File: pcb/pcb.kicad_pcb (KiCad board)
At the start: 2 copper layers, 84 parts, among them J1 MJ-4PP-9, J2 MJ-4PP-9, SW1 KEY_SW, SW10 KEY_SW, SW11 KEY_SW, SW12 KEY_SW, SW13 KEY_SW, SW14 KEY_SW, SW15 KEY_SW, SW16 KEY_SW, SW17 KEY_SW, SW18 KEY_SW, SW19 KEY_SW, SW2 KEY_SW, SW20 KEY_SW, SW21 KEY_SW, SW22 KEY_SW, SW23 KEY_SW, SW24 KEY_SW, SW25 KEY_SW, SW26 KEY_SW, SW27 RotaryEncoder, SW3 KEY_SW, SW30 KEY_SW, SW31 KEY_SW, SW32 KEY_SW, SW33 KEY_SW, SW34 KEY_SW, SW35 KEY_SW, SW36 KEY_SW, SW37 KEY_SW, SW38 KEY_SW, SW39 KEY_SW, SW4 KEY_SW, SW40 KEY_SW, SW41 KEY_SW, SW42 KEY_SW, SW43 KEY_SW, SW44 KEY_SW, SW45 KEY_SW, SW46 KEY_SW, SW47 KEY_SW, SW48 KEY_SW, SW49 KEY_SW, SW5 KEY_SW, SW50 KEY_SW, SW51 KEY_SW, SW52 KEY_SW, SW53 KEY_SW, SW54 KEY_SW, SW55 RotaryEncoder, SW6 KEY_SW, SW7 KEY_SW, SW8 KEY_SW, SW9 KEY_SW, U1 ESP32-S3-WROOM-1, U3 USBLC6-2SC6

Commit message: switch put to pcb
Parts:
- removed SW55: RotaryEncoder, keebio:RotaryEncoder_EC11
- added ?: , , F.Cu at (103.2, 117.0)
- added BT1: Battery_Cell, Connector_JST:JST_XH_S2B-XH-A_1x02_P2.50mm_Horizontal, F.Cu at (20.0, -34.4)
- added C1: 0.1uF, Capacitor_SMD:C_0805_2012Metric_Pad1.18x1.45mm_HandSolder, F.Cu at (225.0, 52.7)
- added C2: 0.1uF, Capacitor_SMD:C_0805_2012Metric_Pad1.18x1.45mm_HandSolder, F.Cu at (229.4, 53.0)
- added C3: 10uF, Capacitor_SMD:C_0805_2012Metric_Pad1.18x1.45mm_HandSolder, F.Cu at (45.5, 10.9)
- added C4: 10uF, Capacitor_SMD:C_0805_2012Metric_Pad1.18x1.45mm_HandSolder, F.Cu at (50.7, 10.5)
- added C5: 4700pF, Capacitor_SMD:C_0603_1608Metric_Pad1.08x0.95mm_HandSolder, F.Cu at (43.7, 48.8)
- added C6: 22uF, Capacitor_SMD:C_0805_2012Metric_Pad1.18x1.45mm_HandSolder, F.Cu at (46.8, 4.81)
- added C7: 0.1uF, Capacitor_SMD:C_0805_2012Metric_Pad1.18x1.45mm_HandSolder, F.Cu at (39.5, 10.0)
- added D28: D, keebio:Diode-dual, F.Cu at (16.6, -17.4)
- added D29: D, keebio:Diode-dual, F.Cu at (48.2, 47.0)
- added J3: USB_C_Receptacle_USB2.0_16P, Connector_USB:USB_C_Receptacle_GCT_USB4105-xx-A_16P_TopMnt_Horizontal, F.Cu at (46.4, 34.5)
- added J4: USB to TTL, Connector_PinSocket_2.54mm:PinSocket_1x06_P2.54mm_Horizontal, F.Cu at (238.1, 74.0)
- added J5: Conn_01x03, lib:StripLED_rev, F.Cu at (178.3, 92.7)
- added J6: Conn_01x03, lib:StripLED_rev, F.Cu at (175.8, 92.7)
- added LED1: YS-SK6812MINI-E, lib:YS-SK6812MINI-E, F.Cu at (107.2, 122.1)
- added LED2: YS-SK6812MINI-E, lib:YS-SK6812MINI-E, F.Cu at (128.7, 116.2)
- added LED3: YS-SK6812MINI-E, lib:YS-SK6812MINI-E, F.Cu at (150.7, 114.3)
- added LED4: YS-SK6812MINI-E, lib:YS-SK6812MINI-E, F.Cu at (174.1, 117.4)
- added LED5: YS-SK6812MINI-E, lib:YS-SK6812MINI-E, F.Cu at (196.0, 126.4)
- added R1: 10kΩ, keebio:Resistor-Hybrid, F.Cu at (226.6, 49.7)
- added R2: 5.1kΩ, keebio:Resistor-Hybrid, F.Cu at (46.9, 42.2)
- added R3: 5.1kΩ, keebio:Resistor-Hybrid, F.Cu at (46.9, 45.3)
- added R4: 1MΩ, keebio:Resistor-Hybrid, F.Cu at (45.9, 40.5)
- added R5: 5.1kΩ, keebio:Resistor-Hybrid, F.Cu at (159.0, 40.8)
- added R6: 5.1kΩ, keebio:Resistor-Hybrid, F.Cu at (174.5, 38.8)
- added REF**: MountingHole_2.2mm_M2, MountingHole:MountingHole_2.2mm_M2, F.Cu at (100.7, 75.2)
- added REF**: MountingHole_2.2mm_M2, MountingHole:MountingHole_2.2mm_M2, F.Cu at (103.1, 94.3)
- added REF**: MountingHole_2.2mm_M2, MountingHole:MountingHole_2.2mm_M2, F.Cu at (185.8, 120.2)
- added REF**: MountingHole_2.2mm_M2, MountingHole:MountingHole_2.2mm_M2, F.Cu at (64.4, 109.2)
- added REF**: MountingHole_2.2mm_M2, MountingHole:MountingHole_2.2mm_M2, F.Cu at (82.4, 76.7)
- added REF**: MountingHole_2.2mm_M2, MountingHole:MountingHole_2.2mm_M2, F.Cu at (60.4, 90.5)
- added REF**: MountingHole_2.2mm_M2, MountingHole:MountingHole_2.2mm_M2, F.Cu at (103.2, 117.0)
- added REF**: MountingHole_2.2mm_M2, MountingHole:MountingHole_2.2mm_M2, F.Cu at (160.3, 94.3)
- added REF**: MountingHole_2.2mm_M2, MountingHole:MountingHole_2.2mm_M2, F.Cu at (179.3, 113.3)
- added REF**: MountingHole_2.2mm_M2, MountingHole:MountingHole_2.2mm_M2, F.Cu at (94.2, 44.2)
- added REF**: MountingHole_2.2mm_M2, MountingHole:MountingHole_2.2mm_M2, F.Cu at (202.3, 98.0)
- added REF**: MountingHole_2.2mm_M2, MountingHole:MountingHole_2.2mm_M2, F.Cu at (157.9, 75.2)
- added REF**: MountingHole_2.2mm_M2, MountingHole:MountingHole_2.2mm_M2, F.Cu at (96.7, 122.3)
- added REF**: MountingHole_2.2mm_M2, MountingHole:MountingHole_2.2mm_M2, F.Cu at (203.8, 45.6)
- added REF**: MountingHole_2.2mm_M2, MountingHole:MountingHole_2.2mm_M2, F.Cu at (176.8, 75.2)
- added RV1: Slider 50kΩ, lib:SL4515NB103L15CM, F.Cu at (118.9, 47.9)
- added SW60: RESET_SW, kbd:ResetSW, F.Cu at (227.8, 58.9)
- added SW61: BOOT_SW, kbd:ResetSW, F.Cu at (251.5, 101.3)
- added SW６２1: DIP_SW, lib:DIPS762W80P254L1170H690Q8N, F.Cu at (189.6, 44.6)
- added U2: TPS1117LV33S, Package_TO_SOT_SMD:SOT-223-3_TabPin2, F.Cu at (46.6, 16.6)
- J1, SW27: moved to B.Cu
- moved U3 206.8 mm to (76.2, 37.8)
- moved D15 188.5 mm to (54.9, 110.1), turned to 5 degrees
- moved D1 183.1 mm to (50.9, 91.3), turned to 5 degrees
- moved D8 173.3 mm to (62.4, 100.6), turned to 95 degrees
- moved D16 170.1 mm to (73.9, 108.4), turned to 5 degrees
- moved D2 165.0 mm to (69.9, 89.6), turned to 5 degrees
- moved D9 155.7 mm to (81.4, 98.9), turned to 95 degrees
- moved D17 153.8 mm to (93.6, 94.3)
- moved D3 148.4 mm to (91.2, 75.2)
- moved D10 141.6 mm to (101.8, 84.7), turned to -90 degrees
- moved D18 136.1 mm to (112.6, 94.3)
- moved D22 135.6 mm to (117.9, 127.3), turned to -70 degrees
- moved D4 131.3 mm to (110.2, 75.2)
- moved D11 125.7 mm to (120.9, 84.7), turned to -90 degrees
- moved D19 119.0 mm to (131.7, 94.3)
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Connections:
- J1 pad A: unconnected-(J1-PadA) -> split toggle
- J2 pad A: unconnected-(J1-PadA) -> split toggle
- U1 pad 12: unconnected-(U1-IO8-Pad12) -> col6
- U1 pad 15: col2 -> col1
- U1 pad 17: unconnected-(U1-IO9-Pad17) -> power toggle
- U1 pad 18: unconnected-(U1-IO10-Pad18) -> BLE toggle
- U1 pad 19: unconnected-(U1-IO11-Pad19) -> LED toggle
- U1 pad 27: Net-(U1-IO0) -> IO0
- U1 pad 3: Net-(U1-EN) -> EN
- U1 pad 35: unconnected-(U1-IO42-Pad35) -> rgb-led
- U1 pad 38: col1 -> col0
- U1 pad 39: col0 -> slider
- U1 pad 4: col3 -> col2
- U1 pad 5: col4 -> col3
- U1 pad 6: col5 -> col4
- U1 pad 7: col6 -> col5
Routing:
- net GND: track 0.00 -> 158.6 mm, vias 0 -> 2
- net row0: track 0.00 -> 130.6 mm
- net row2: track 0.00 -> 130.2 mm
- net +3V3: track 0.00 -> 129.9 mm, vias 0 -> 5
- net row1: track 0.00 -> 113.8 mm
- net row3: track 0.00 -> 108.4 mm
- net col3: track 0.00 -> 98.8 mm, vias 0 -> 4
- net col4: track 0.00 -> 92.3 mm, vias 0 -> 4
- net col5: track 0.00 -> 88.5 mm, vias 0 -> 4
- net Net-(J5-Pin_2): track 0.00 -> 76.9 mm, vias 0 -> 1
- net col6: track 0.00 -> 70.3 mm, vias 0 -> 3
- net col2: track 0.00 -> 60.4 mm, vias 0 -> 3
- net Net-(D17-A): track 0.00 -> 37.3 mm, vias 0 -> 1
- net Net-(D18-A): track 0.00 -> 37.3 mm, vias 0 -> 1
- net Net-(D19-A): track 0.00 -> 37.3 mm, vias 0 -> 1
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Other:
- board outline added: 174.6 x 103.7 mm

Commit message: ESP32 put to pcb
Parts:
- C1, C2: footprint Capacitor_SMD:C_0805_2012Metric_Pad1.18x1.45mm_HandSolder -> lib:C_0805_2012Metric_Pad1.18x1.45mm_HandSolder_rev
- J4: moved to B.Cu
- moved C7 169.0 mm to (198.2, 68.0)
- moved C6 163.4 mm to (198.2, 66.0)
- moved C3 161.7 mm to (198.2, 64.0)
- moved C4 155.3 mm to (195.4, 67.1), turned to -90 degrees
- moved U2 151.9 mm to (190.0, 66.7), turned to 180 degrees
- moved U3 126.7 mm to (202.8, 34.2)
- moved BT1 104.3 mm to (79.3, 51.3), turned to -145 degrees
- moved J4 101.0 mm to (138.6, 56.9), turned to -90 degrees
- moved D28 76.4 mm to (81.2, 23.4)
- moved SW61 68.1 mm to (196.2, 61.5)
- moved J3 63.2 mm to (108.2, 21.6), turned to 180 degrees
- moved R1 53.3 mm to (173.8, 57.1)
- moved R2 52.2 mm to (98.8, 47.7)
- moved R4 51.8 mm to (97.5, 45.5)
- moved R3 51.4 mm to (98.1, 50.3)
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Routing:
- net col0: track 24.8 -> 204.6 mm, vias 2 -> 4
- net col1: track 19.6 -> 174.4 mm, vias 1 -> 5
- net rgb-led: track 0.00 -> 128.7 mm, vias 0 -> 3
- net GND: track 158.6 -> 220.0 mm, vias 2 -> 6
- net row0: track 130.6 -> 159.0 mm
- net row3: track 108.4 -> 136.2 mm, vias 0 -> 1
- net row2: track 130.2 -> 151.2 mm
- net Net-(J5-Pin_2): track 76.9 -> 56.6 mm, vias 1 -> 3
- net row1: track 113.8 -> 126.5 mm
- net Net-(D9-A): track 2.61 -> 13.4 mm
- net Net-(D8-A): track 2.62 -> 13.4 mm
- net EN: track 0.00 -> 10.5 mm
- net +3V3: track 129.9 -> 139.3 mm
- net /VBUS: track 0.00 -> 4.19 mm
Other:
- board size 174.6 x 103.7 mm -> 168.9 x 103.7 mm

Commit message: connect
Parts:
- J3: footprint Connector_USB:USB_C_Receptacle_GCT_USB4105-xx-A_16P_TopMnt_Horizontal -> lib:USB_C_Receptacle_GCT_USB4105-xx-A_16P_TopMnt_Horizontal_rev
- moved D28 62.7 mm to (133.8, 57.4)
- moved D29 47.8 mm to (144.8, 57.4)
- moved U3 38.3 mm to (182.5, 66.7), turned to 90 degrees
- moved R5 29.6 mm to (186.8, 60.4), turned to 180 degrees
- moved R4 27.7 mm to (122.5, 57.4)
- moved J3 25.5 mm to (111.7, 46.8)
- moved BT1 24.3 mm to (103.6, 50.7), turned to -90 degrees
- moved R6 19.3 mm to (186.8, 56.4)
- moved REF** 15.7 mm to (102.4, 45.6)
- moved R3 15.5 mm to (111.7, 57.7), turned to 180 degrees
- moved R2 15.2 mm to (111.7, 55.6), turned to 180 degrees
- moved C5 14.2 mm to (105.6, 52.0), turned to -90 degrees
- moved J4 14.2 mm to (152.8, 57.4)
- moved R1 13.0 mm to (186.8, 58.4)
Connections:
- U1 pad 12: col6 -> power toggle
- U1 pad 15: col1 -> slider
- U1 pad 17: power toggle -> col6
- U1 pad 18: BLE toggle -> col5
- U1 pad 19: LED toggle -> col4
- U1 pad 20: unconnected-(U1-IO12-Pad20) -> col3
- U1 pad 21: unconnected-(U1-IO13-Pad21) -> col2
- U1 pad 39: slider -> col1
- U1 pad 4: col2 -> unconnected-(U1-IO4-Pad4)
- U1 pad 5: col3 -> unconnected-(U1-IO5-Pad5)
- U1 pad 6: col4 -> LED toggle
- U1 pad 7: col5 -> BLE toggle
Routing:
- net GND: track 220.0 -> 412.0 mm, vias 6 -> 13
- net col2: track 60.4 -> 165.6 mm, vias 3 -> 5
- net Net-(D29-A): track 0.00 -> 91.2 mm, vias 0 -> 5
- net col3: track 98.8 -> 188.7 mm, vias 4 -> 5
- net +3V3: track 139.3 -> 226.9 mm, vias 5 -> 7
- net Net-(J3-D+-PadA6): track 0.00 -> 87.4 mm, vias 0 -> 2
- net Net-(J3-D--PadA7): track 0.00 -> 85.7 mm, vias 0 -> 2
- net slider: track 0.00 -> 82.6 mm, vias 0 -> 1
- net /VBUS: track 4.19 -> 77.9 mm, vias 0 -> 2
- net Net-(R5-Pad1): track 0.00 -> 72.3 mm
- net IO0: track 0.00 -> 70.5 mm, vias 0 -> 2
- net EN: track 10.5 -> 80.3 mm, vias 0 -> 3
- net USB-TX: track 0.00 -> 68.4 mm, vias 0 -> 2
- net col4: track 92.3 -> 154.6 mm, vias 4 -> 6
- net USB-RX: track 0.00 -> 54.9 mm, vias 0 -> 2
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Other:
- outline, holes or cut-outs redrawn

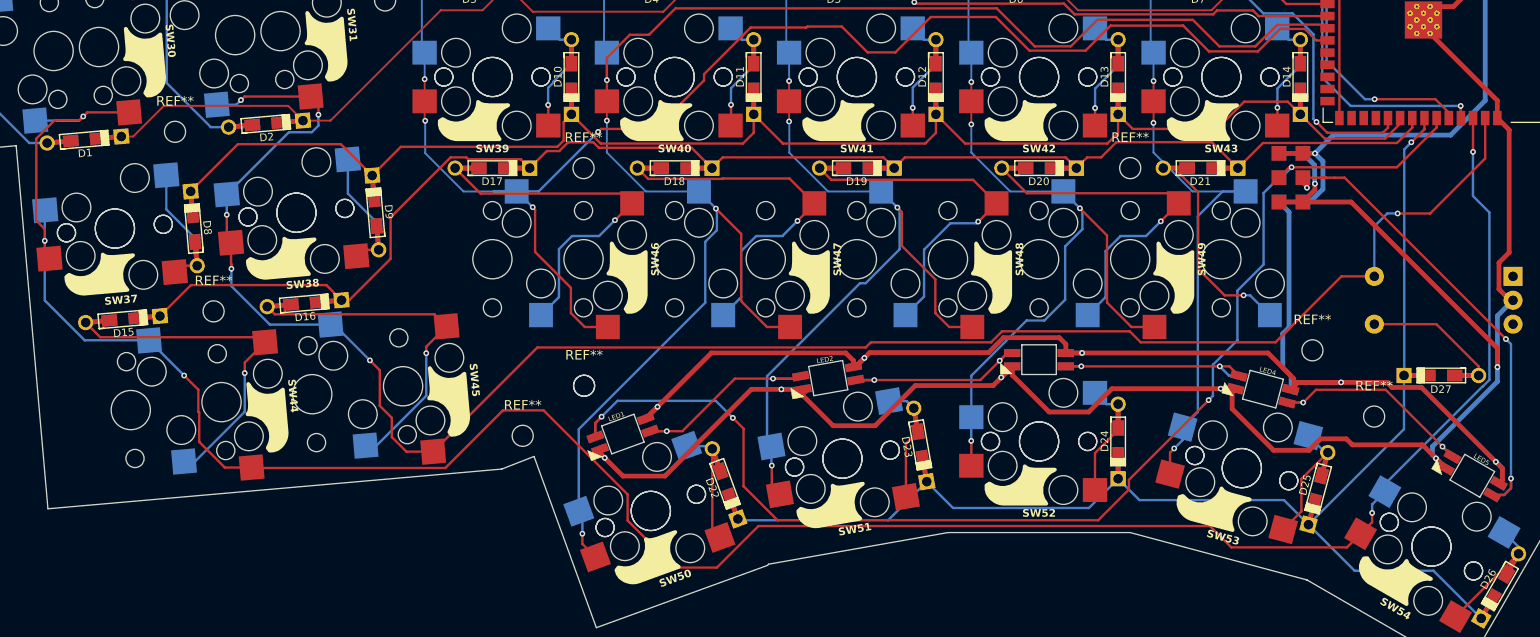
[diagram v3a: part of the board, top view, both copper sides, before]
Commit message: fix DRC error of switch
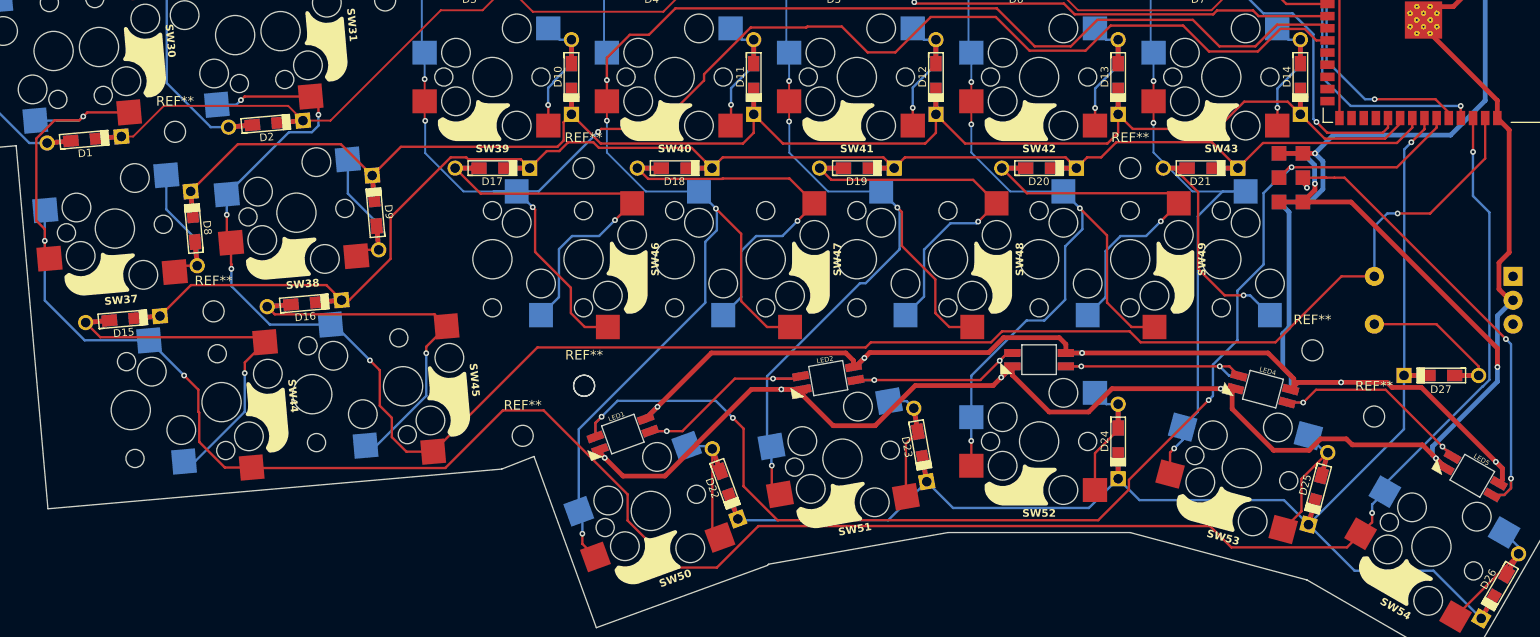
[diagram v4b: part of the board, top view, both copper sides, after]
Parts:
- SW10, SW11, SW12, SW13, SW14, SW22, SW23, SW24, SW25, SW26, SW8, SW9: footprint kbd:keyswitch_cherrymx_hotswap_1u -> lib:keyswitch_cherrymx_hotswap_1u_no_hole

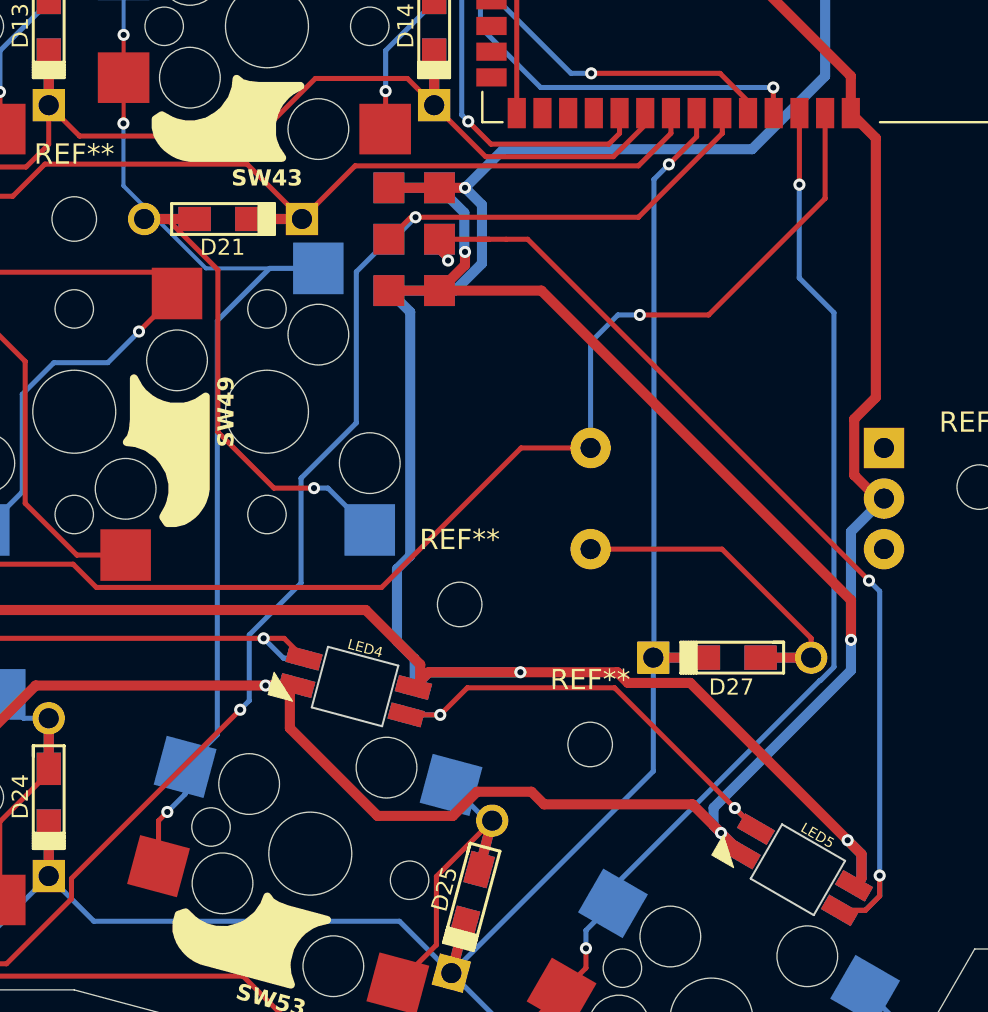
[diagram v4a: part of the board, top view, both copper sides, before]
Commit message: fix DRC error of LED
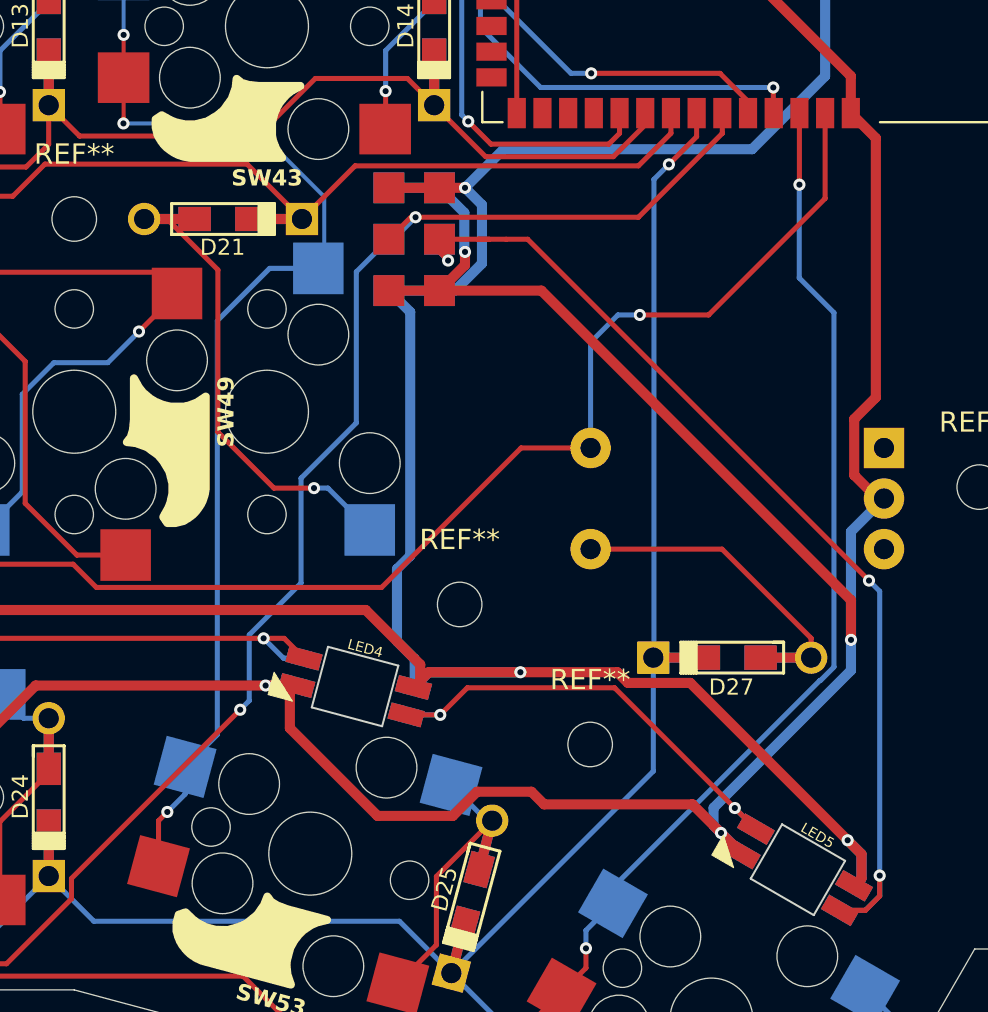
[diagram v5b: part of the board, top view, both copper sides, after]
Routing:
- net col6: track 93.8 -> 94.5 mm
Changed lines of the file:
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@@
-	)
-	(segment
-		(start 199.159293 126.85894)
-		(end 199.159293 125.653263)
-		(width 0.5)
-		(layer "B.Cu")
-		(net 35)
 	)
 	(segment
@@
 	)
 	(segment
+		(start 198.478554 124.972524)
+		(end 199.159293 125.653263)
+		(width 0.5)
+		(layer "B.Cu")
+		(net 35)
+	)
+	(segment
 		(start 176.204776 115.135344)
 		(end 177.078139 116.008707)
@@
 	)
 	(segment
-		(start 199.159293 125.653263)
-		(end 198.478554 124.972524)
-		(width 0.5)
-		(layer "B.Cu")
-		(net 35)
-	)
-	(segment
 		(start 177.763845 116.677317)
 		(end 182.294767 116.677317)
@@
 	)
 	(segment
+		(start 199.159293 125.653263)
+		(end 199.159293 126.85894)
+		(width 0.5)
+		(layer "B.Cu")
+		(net 35)
+	)
+	(segment
 		(start 181.476782 90.817318)
 		(end 179.566778 92.727322)
@@
 	)
 	(segment
-		(start 198.795469 127.222764)
-		(end 199.159293 126.85894)
-		(width 0.5)
-		(layer "B.Cu")
-		(net 35)
-	)
-	(segment
 		(start 176.859753 110.912341)
 		(end 176.204776 111.567318)
@@
 	)
 	(segment
+		(start 199.159293 126.85894)
+		(end 198.795469 127.222764)
+		(width 0.5)
+		(layer "B.Cu")
+		(net 35)
+	)
+	(segment
 		(start 193.124776 55.725085)
 		(end 193.124776 53.267318)
@@
 	)
 	(segment
-		(start 166.764113 96.707317)
-		(end 172.319753 96.707317)
+		(start 168.98593 89.543499)
+		(end 162.684999 89.543499)
+		(width 0.2)
+		(layer "B.Cu")
+		(net 42)
+	)
+	(segment
+		(start 172.609753 93.167322)
+		(end 168.98593 89.543499)
 		(width 0.2)
 		(layer "B.Cu")
@@
 	)
 	(segment
-		(start 162.684999 89.543499)
-		(end 162.684999 92.628203)
+		(start 172.609753 96.417317)
+		(end 172.609753 93.167322)
 		(width 0.2)
 		(layer "B.Cu")
@@
 	)
 	(segment
-		(start 162.684999 92.628203)
-		(end 166.764113 96.707317)
-		(width 0.2)
-		(layer "B.Cu")
-		(net 42)
-	)
-	(segment
 		(start 162.694753 85.167295)
 		(end 162.694753 82.202322)
@@
 		(layer "B.Cu")
 		(net 42)
+	)
+	(segment
+		(start 172.319753 96.707317)
+		(end 172.609753 96.417317)
+		(width 0.2)
+		(layer "B.Cu")
+		(net 42)
